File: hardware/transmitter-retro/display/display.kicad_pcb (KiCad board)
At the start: 2 copper layers, 100 x 90 mm, 48 parts, among them J4 Expansion, U1 74LS163, U10 74LS08, U11 74LS08, U12 74LS00, U14 74LS10, U15 74LS32, U16 74LS32, U2 74LS74, U3 74LS162, U4 74LS163, U5 74LS163, U6 74LS161, U7 74LS161, U8 74LS157, U9 74LS08

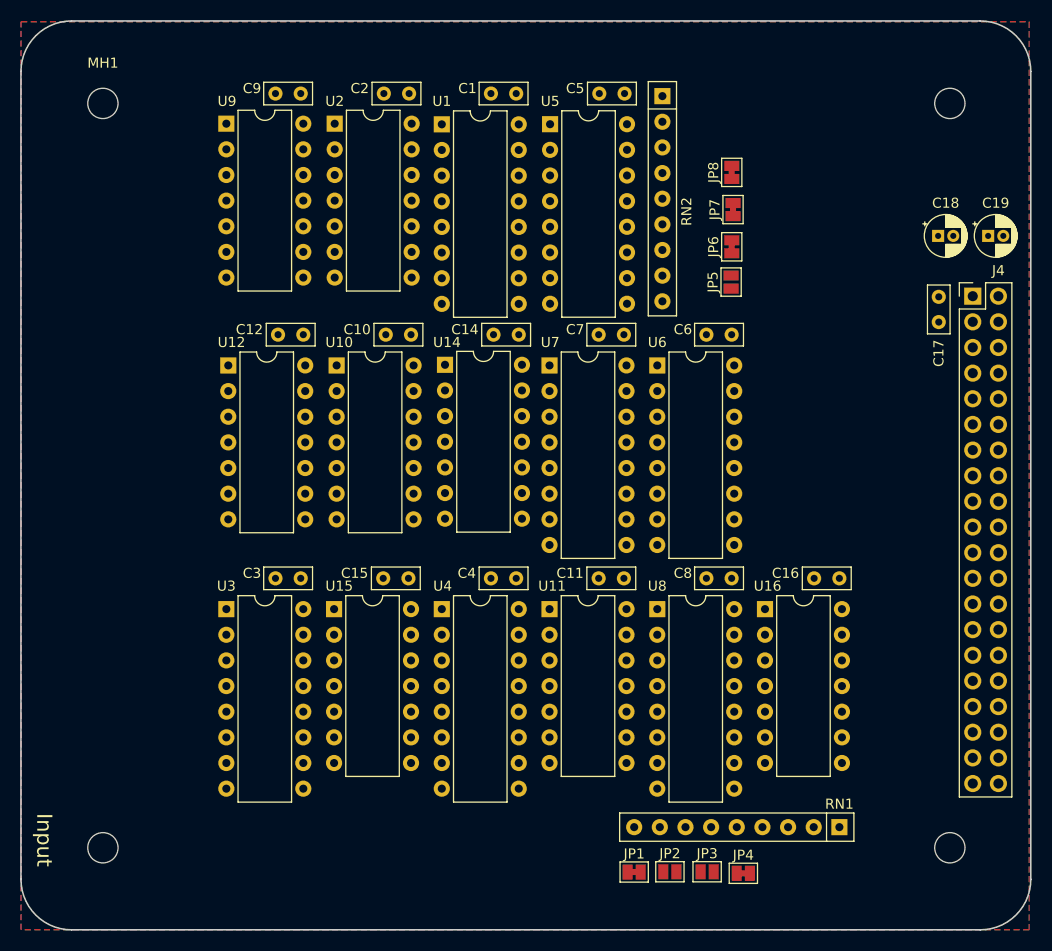
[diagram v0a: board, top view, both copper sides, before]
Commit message: Prototype and PCB layout for core Prototype and PCB layout for demo Prototype and PCB layout for control-eprom Move display design forward Refactor control-dmx to dmx Update expansion connector on all boards Add test suites Add tx-retro readme Cleanup
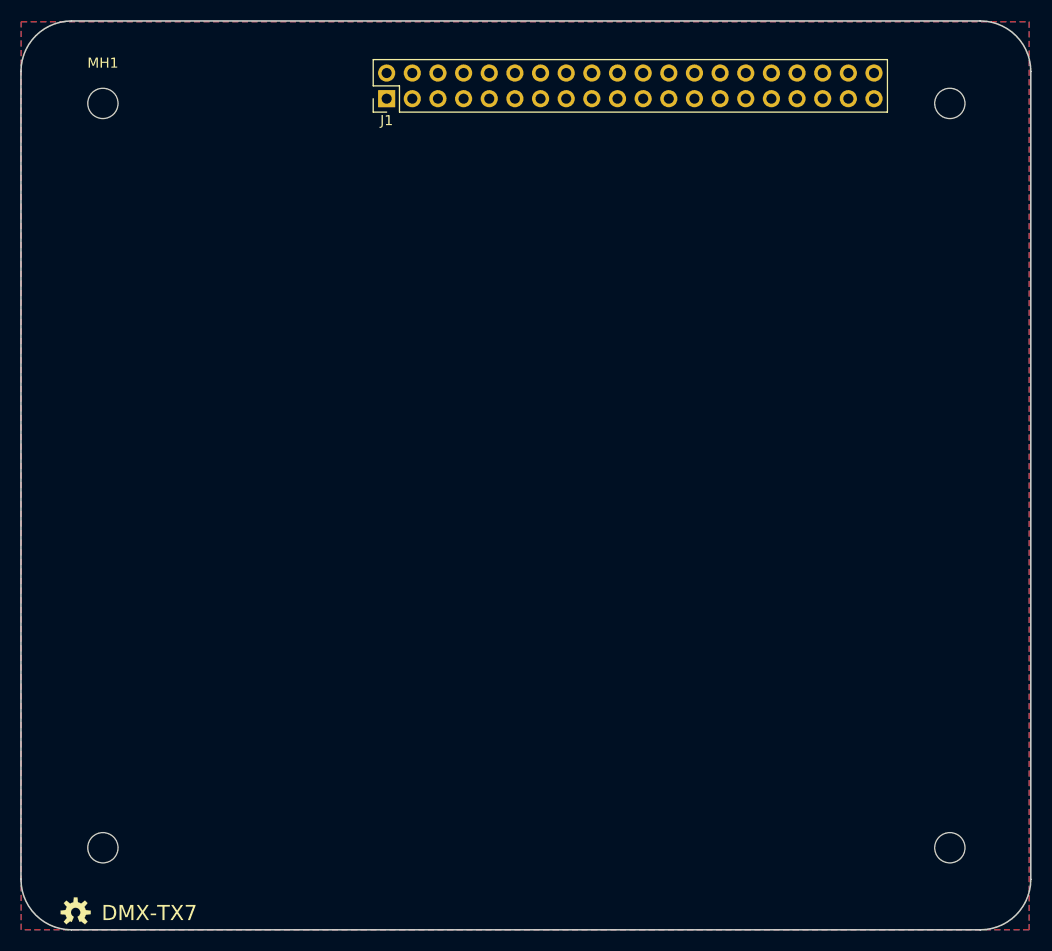
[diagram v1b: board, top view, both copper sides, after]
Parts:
- removed C1, C10, C11, C12, C14, C15, C16, C17, C2, C3, C4, C5, C6, C7, C8, C9: .01uF, Capacitor_THT:C_Rect_L4.6mm_W2.0mm_P2.50mm_MKS02_FKP02
- removed C18, C19: CP1, Capacitor_THT:CP_Radial_D4.0mm_P1.50mm
- removed J4: Expansion, Connector_PinHeader_2.54mm:PinHeader_2x20_P2.54mm_Vertical
- removed JP1: RC0, Jumper:SolderJumper-2_P1.3mm_Bridged_Pad1.0x1.5mm
- removed JP2: RC1, Jumper:SolderJumper-2_P1.3mm_Open_Pad1.0x1.5mm
- removed JP3: RC2, Jumper:SolderJumper-2_P1.3mm_Open_Pad1.0x1.5mm
- removed JP4: RC3, Jumper:SolderJumper-2_P1.3mm_Bridged_Pad1.0x1.5mm
- removed JP5: PB0, Jumper:SolderJumper-2_P1.3mm_Open_Pad1.0x1.5mm
- removed JP6: PB1, Jumper:SolderJumper-2_P1.3mm_Bridged_Pad1.0x1.5mm
- removed JP7: PB2, Jumper:SolderJumper-2_P1.3mm_Bridged_Pad1.0x1.5mm
- removed JP8: PB3, Jumper:SolderJumper-2_P1.3mm_Bridged_Pad1.0x1.5mm
- removed RN1, RN2: 10k, Resistor_THT:R_Array_SIP9
- removed U1, U4, U5: 74LS163, Package_DIP:DIP-16_W7.62mm
- removed U10, U11, U9: 74LS08, Package_DIP:DIP-14_W7.62mm
- removed U12: 74LS00, Package_DIP:DIP-14_W7.62mm
- removed U14: 74LS10, Package_DIP:DIP-14_W7.62mm
- removed U15, U16: 74LS32, Package_DIP:DIP-14_W7.62mm
- removed U2: 74LS74, Package_DIP:DIP-14_W7.62mm
- removed U3: 74LS162, Package_DIP:DIP-16_W7.62mm
- removed U6, U7: 74LS161, Package_DIP:DIP-16_W7.62mm
- removed U8: 74LS157, Package_DIP:DIP-16_W7.62mm
- added ?: , footprints:OSHW-LOGO-S, F.Cu at (92.5, 137.0)
- added G***: LOGO, footprints:logo_cr_5x5, B.Cu at (105.7, 131.6)
- added J1: Expansion, Connector_PinHeader_2.54mm:PinHeader_2x20_P2.54mm_Vertical, F.Cu at (123.3, 56.4)
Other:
- net class Default: trace_width 0.25 -> 0.127
- net class Gnd added: clearance 0.25, trace_width 0.75, via_dia 0.8, via_drill 0.4
- net class Power added: clearance 0.25, trace_width 0.75, via_dia 0.8, via_drill 0.4
- rule trace_min: 0.2 -> 0.127
- rule via_min_size: 0.4 -> 0.5
- board text added: "DMX-TX7"
- board text added: "DMX-TX7, Rev 0.9 Crazy Giraffe Software"
- board text removed: "DMX-CPCB, Rev 1.2 Crazy Giraffe Software"
- board text removed: "Input"
